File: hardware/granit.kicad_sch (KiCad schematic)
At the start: 0 parts

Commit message: Rename project to Granit
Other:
- company: https://github.com/laenzlinger/offsite-backup -> https://github.com/laenzlinger/granit
- title: Offsite Backup Device -> Granit — Offsite Backup Device
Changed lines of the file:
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@@
 	(paper "A4")
 	(title_block
-		(title "Offsite Backup Device")
+		(title "Granit — Offsite Backup Device")
 		(date "2026-04-07")
 		(rev "0.1")
-		(company "https://github.com/laenzlinger/offsite-backup")
+		(company "https://github.com/laenzlinger/granit")
 		(comment 1 "License: CERN Open Hardware Licence Version 2 - Permissive")
 		(comment 2 "Git commit hash: ${GIT_HASH}")
@@
 		)
 		(instances
-			(project "offsite-backup"
+			(project "granit"
 				(path "/d2c135e3-a983-4cd4-8cff-b50ca3c7671a"
 					(page "2")
@@
 		)
 		(instances
-			(project "offsite-backup"
+			(project "granit"
 				(path "/d2c135e3-a983-4cd4-8cff-b50ca3c7671a"
 					(page "3")
@@
 		)
 		(instances
-			(project "offsite-backup"
+			(project "granit"
 				(path "/d2c135e3-a983-4cd4-8cff-b50ca3c7671a"
 					(page "4")

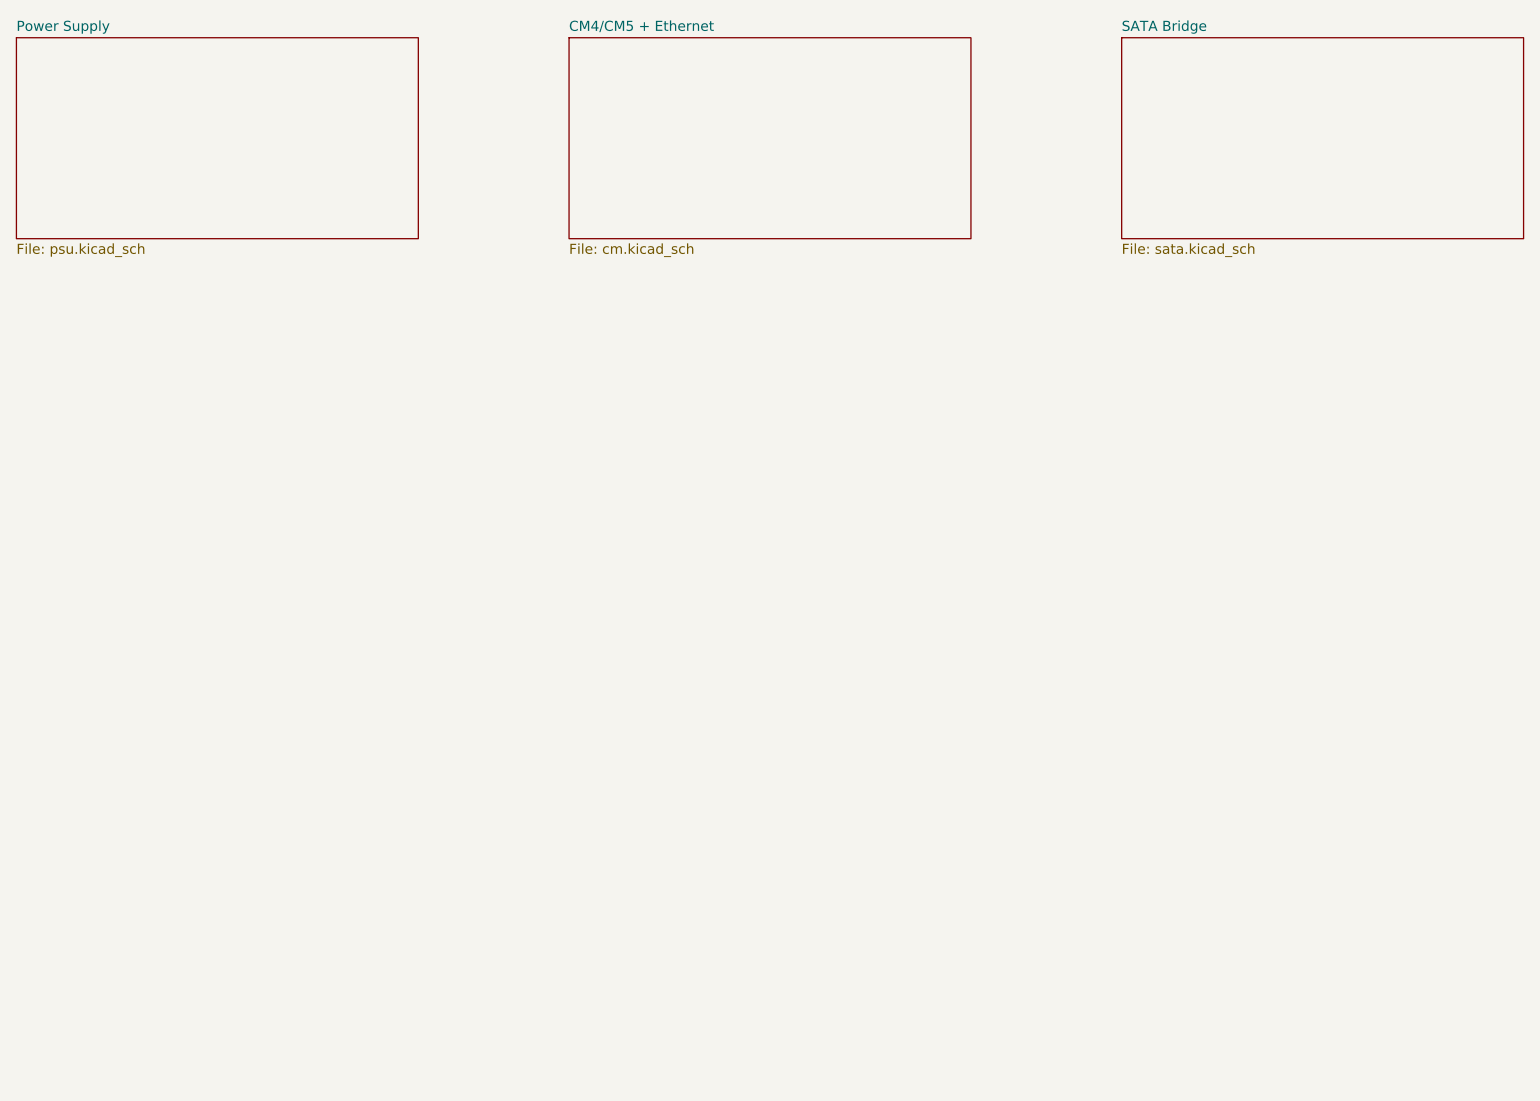
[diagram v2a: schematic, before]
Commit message: Split CM4 into separate connector sheets, add peripherals sheet
Sheet structure:
- psu.kicad_sch          (Power Supply)
- cm-conn1.kicad_sch     (CM4 Connector 1: power, USB, HDMI)
- cm-conn2.kicad_sch     (CM4 Connector 2: PCIe, Ethernet, GPIO, I2C)
- sata.kicad_sch         (ASM1061 PCIe-to-SATA)
- peripherals.kicad_sch  (RTC, LED, button)
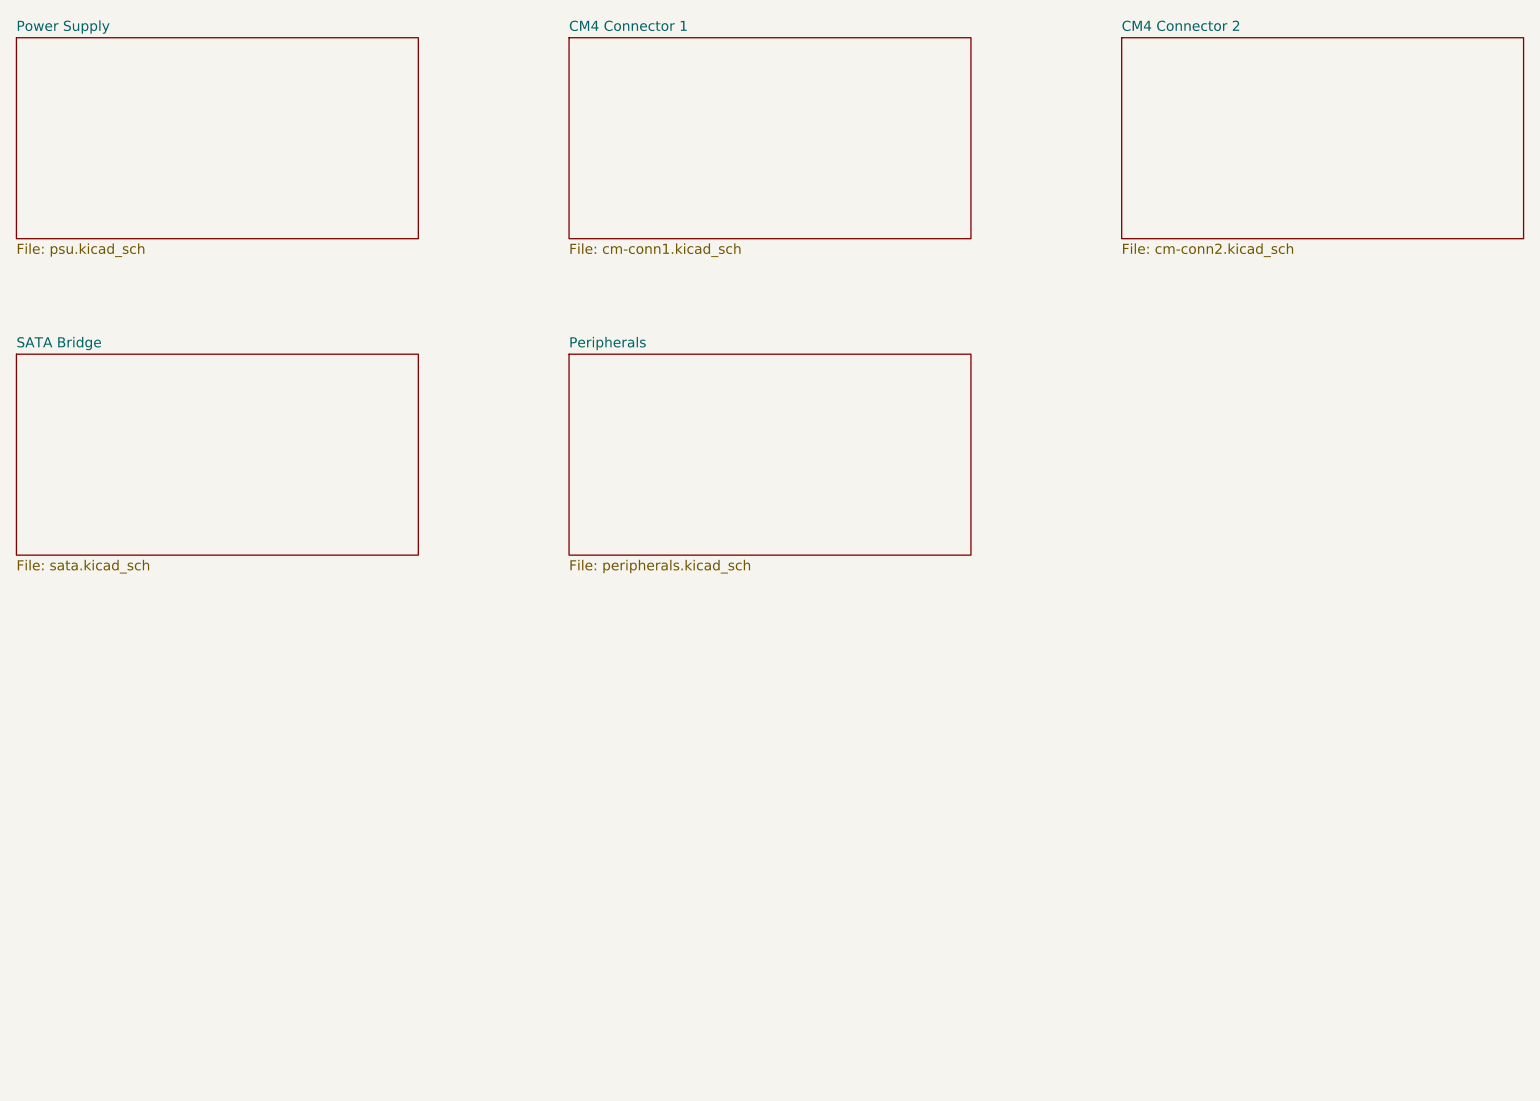
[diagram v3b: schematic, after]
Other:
- sheet CM4/CM5 + Ethernet renamed CM4 Connector 1
- added sheet CM4 Connector 2 (cm-conn2.kicad_sch)
- added sheet Peripherals (peripherals.kicad_sch)
- sheet CM4 Connector 1: file cm.kicad_sch -> cm-conn1.kicad_sch
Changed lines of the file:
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@@
-	)
-	(sheet
-		(at 100.33 30.48)
-		(size 50.8 25.4)
-		(exclude_from_sim no)
-		(in_bom yes)
-		(on_board yes)
-		(dnp no)
-		(fields_autoplaced yes)
-		(stroke
-			(width 0.1524)
-			(type solid)
-		)
-		(fill
-			(color 0 0 0 0)
-		)
-		(property "Sheetname" "CM4/CM5 + Ethernet"
-			(at 100.33 29.7684 0)
-			(show_name no)
-			(do_not_autoplace no)
-			(effects
-				(font
-					(size 1.27 1.27)
-				)
-				(justify left bottom)
-			)
-		)
-		(property "Sheetfile" "cm.kicad_sch"
-			(at 100.33 56.4646 0)
-			(show_name no)
-			(do_not_autoplace no)
-			(effects
-				(font
-					(size 1.27 1.27)
-				)
-				(justify left top)
-			)
-		)
-		(instances
-			(project "granit"
-				(path "/d2c135e3-a983-4cd4-8cff-b50ca3c7671a"
-					(page "3")
-				)
-			)
-		)
 	)
 	(sheet
@@
 	)
 	(sheet
+		(at 100.33 30.48)
+		(size 50.8 25.4)
+		(exclude_from_sim no)
+		(in_bom yes)
+		(on_board yes)
+		(dnp no)
+		(fields_autoplaced yes)
+		(stroke
+			(width 0.1524)
+			(type solid)
+		)
+		(fill
+			(color 0 0 0 0)
+		)
+		(property "Sheetname" "CM4 Connector 1"
+			(at 100.33 29.7684 0)
+			(show_name no)
+			(do_not_autoplace no)
+			(effects
+				(font
+					(size 1.27 1.27)
+				)
+				(justify left bottom)
+			)
+		)
+		(property "Sheetfile" "cm-conn1.kicad_sch"
+			(at 100.33 56.4646 0)
+			(show_name no)
+			(do_not_autoplace no)
+			(effects
+				(font
+					(size 1.27 1.27)
+				)
+				(justify left top)
+			)
+		)
+		(instances
+			(project "granit"
+				(path "/d2c135e3-a983-4cd4-8cff-b50ca3c7671a"
+					(page "3")
+				)
+			)
+		)
+	)
+	(sheet
 		(at 170.18 30.48)
 		(size 50.8 25.4)
@@
 			(color 0 0 0 0)
 		)
+		(property "Sheetname" "CM4 Connector 2"
+			(at 170.18 29.7684 0)
+			(show_name no)
+			(do_not_autoplace no)
+			(effects
+				(font
+					(size 1.27 1.27)
+				)
+				(justify left bottom)
+			)
+		)
+		(property "Sheetfile" "cm-conn2.kicad_sch"
+			(at 170.18 56.4646 0)
+			(show_name no)
+			(do_not_autoplace no)
+			(effects
+				(font
+					(size 1.27 1.27)
+				)
+				(justify left top)
+			)
+		)
+		(instances
+			(project "granit"
+				(path "/d2c135e3-a983-4cd4-8cff-b50ca3c7671a"
+					(page "4")
+				)
+			)
+		)
+	)
+	(sheet
+		(at 30.48 70.48)
+		(size 50.8 25.4)
+		(exclude_from_sim no)
+		(in_bom yes)
+		(on_board yes)
+		(dnp no)
+		(fields_autoplaced yes)
+		(stroke
+			(width 0.1524)
+			(type solid)
+		)
+		(fill
+			(color 0 0 0 0)
+		)
 		(property "Sheetname" "SATA Bridge"
-			(at 170.18 29.7684 0)
+			(at 30.48 69.7684 0)
 			(show_name no)
 			(do_not_autoplace no)
@@
 		)
 		(property "Sheetfile" "sata.kicad_sch"
-			(at 170.18 56.4646 0)
-			(show_name no)
-			(do_not_autoplace no)
-			(effects
-				(font
-					(size 1.27 1.27)
-				)
-				(justify left top)
-			)
-		)
-		(instances
-			(project "granit"
-				(path "/d2c135e3-a983-4cd4-8cff-b50ca3c7671a"
-					(page "4")
-				)
-			)
+			(at 30.48 96.4646 0)
+			(show_name no)
+			(do_not_autoplace no)
+			(effects
+				(font
+					(size 1.27 1.27)
+				)
+				(justify left top)
+			)
+		)
+		(instances
+			(project "granit"
+				(path "/d2c135e3-a983-4cd4-8cff-b50ca3c7671a"
+					(page "5")
+				)
+			)
+		)
+	)
+	(sheet
+		(at 100.33 70.48)
+		(size 50.8 25.4)
+		(exclude_from_sim no)
+		(in_bom yes)
+		(on_board yes)
+		(dnp no)
+		(fields_autoplaced yes)
+		(stroke
+			(width 0.1524)
+			(type solid)
+		)
+		(fill
+			(color 0 0 0 0)
+		)
+		(property "Sheetname" "Peripherals"
+			(at 100.33 69.7684 0)
+			(show_name no)
+			(do_not_autoplace no)
+			(effects
+				(font
+					(size 1.27 1.27)
+				)
+				(justify left bottom)
+			)
+		)
+		(property "Sheetfile" "peripherals.kicad_sch"
+			(at 100.33 96.4646 0)
+			(show_name no)
+			(do_not_autoplace no)
+			(effects
+				(font
+					(size 1.27 1.27)
+				)
+				(justify left top)
+			)
+		)
+		(instances
+			(project "granit"
+				(path "/d2c135e3-a983-4cd4-8cff-b50ca3c7671a"
+					(page "6")
+				)
+			)

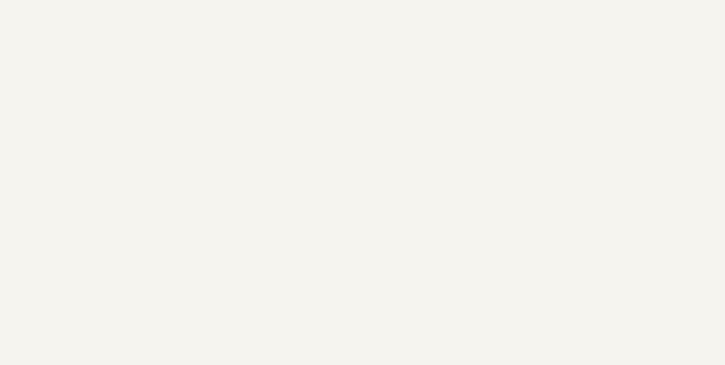
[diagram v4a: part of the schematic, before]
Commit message: Assign fiducial footprints (Fiducial_1mm_Dia_2mm_Outer)
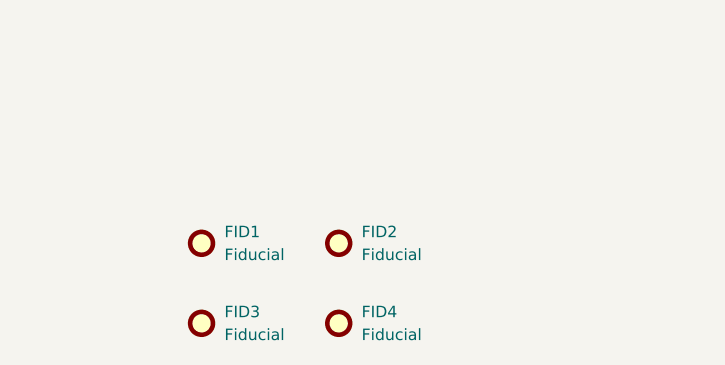
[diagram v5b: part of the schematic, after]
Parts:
- added FID1, FID2, FID3, FID4: Fiducial, Fiducial:Fiducial_1mm_Dia_2mm_Outer, symbol Mechanical:Fiducial

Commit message: Fix fiducial footprint name to Fiducial_1mm_Mask2mm
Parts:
- FID1, FID2, FID3, FID4: footprint Fiducial:Fiducial_1mm_Dia_2mm_Outer -> Fiducial:Fiducial_1mm_Mask2mm
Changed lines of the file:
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@@
 			)
 		)
-		(property "Footprint" "Fiducial:Fiducial_1mm_Dia_2mm_Outer"
+		(property "Footprint" "Fiducial:Fiducial_1mm_Mask2mm"
 			(at 50.8 154.94 0)
 			(hide yes)
@@
 			)
 		)
-		(property "Footprint" "Fiducial:Fiducial_1mm_Dia_2mm_Outer"
+		(property "Footprint" "Fiducial:Fiducial_1mm_Mask2mm"
 			(at 66.04 146.05 0)
 			(hide yes)
@@
 			)
 		)
-		(property "Footprint" "Fiducial:Fiducial_1mm_Dia_2mm_Outer"
+		(property "Footprint" "Fiducial:Fiducial_1mm_Mask2mm"
 			(at 50.8 146.05 0)
 			(hide yes)
@@
 			)
 		)
-		(property "Footprint" "Fiducial:Fiducial_1mm_Dia_2mm_Outer"
+		(property "Footprint" "Fiducial:Fiducial_1mm_Mask2mm"
 			(at 66.04 154.94 0)
 			(hide yes)

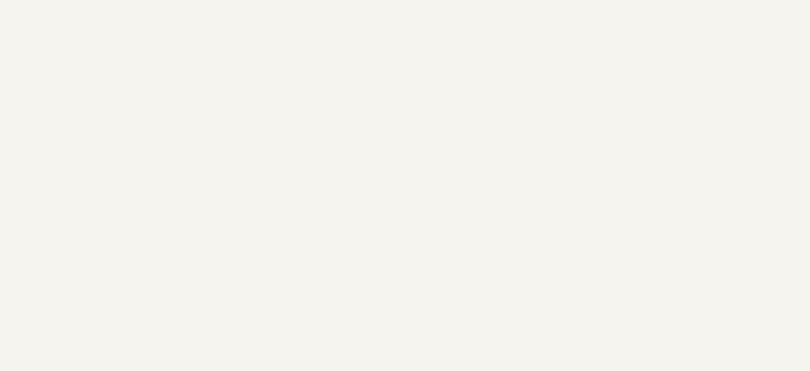
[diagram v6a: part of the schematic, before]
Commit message: Link mounting holes H1-H4 between schematic and PCB, remove redundant DRC exclusions from DESIGN.md
- Set footprint assignments for H1-H4 in schematic
- Add path/sheetname/sheetfile/attr to H1-H4 PCB footprints
- Set Description field on PCB footprints to match schematic
- Remove DRC Exclusions section from DESIGN.md (justifications
  live in kicad_pro exclusion comments)
- Resolves all schematic parity issues (0 remaining)
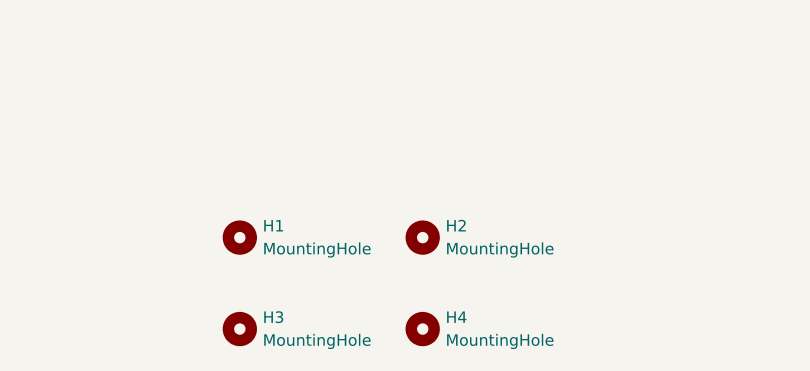
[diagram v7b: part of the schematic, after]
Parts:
- added H1, H2, H3, H4: MountingHole, MountingHole:MountingHole_3.2mm_M3_Pad_Via, symbol Mechanical:MountingHole

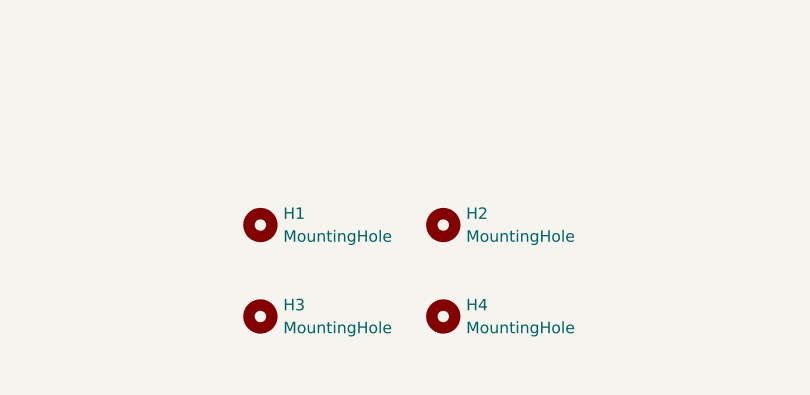
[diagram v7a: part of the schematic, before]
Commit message: Connect mounting holes H1-H4 to GND
- Change symbols from MountingHole to MountingHole_Pad
- Wire pad to GND for chassis ground through metal standoffs
- Update PCB from schematic to sync nets and fields
- ERC clean, 0 schematic parity issues
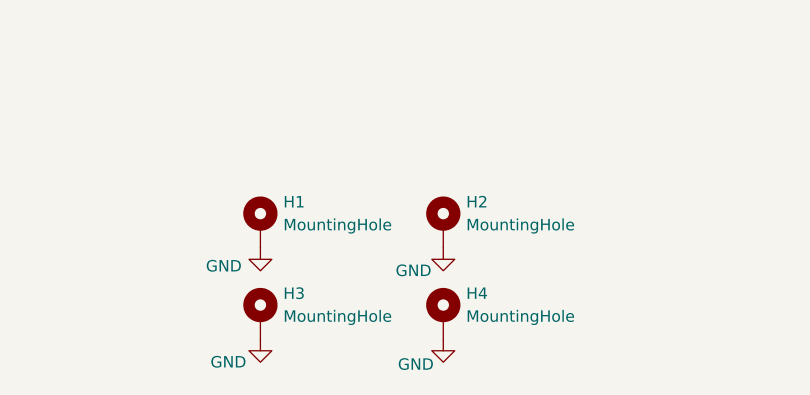
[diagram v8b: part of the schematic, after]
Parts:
- H1, H2, H3, H4: symbol Mechanical:MountingHole -> Mechanical:MountingHole_Pad
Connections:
- new net GND: H1.1, H2.1, H3.1, H4.1
